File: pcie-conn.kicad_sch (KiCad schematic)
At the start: 22 parts, among them J2 Bus_M.2_1-2199230-6

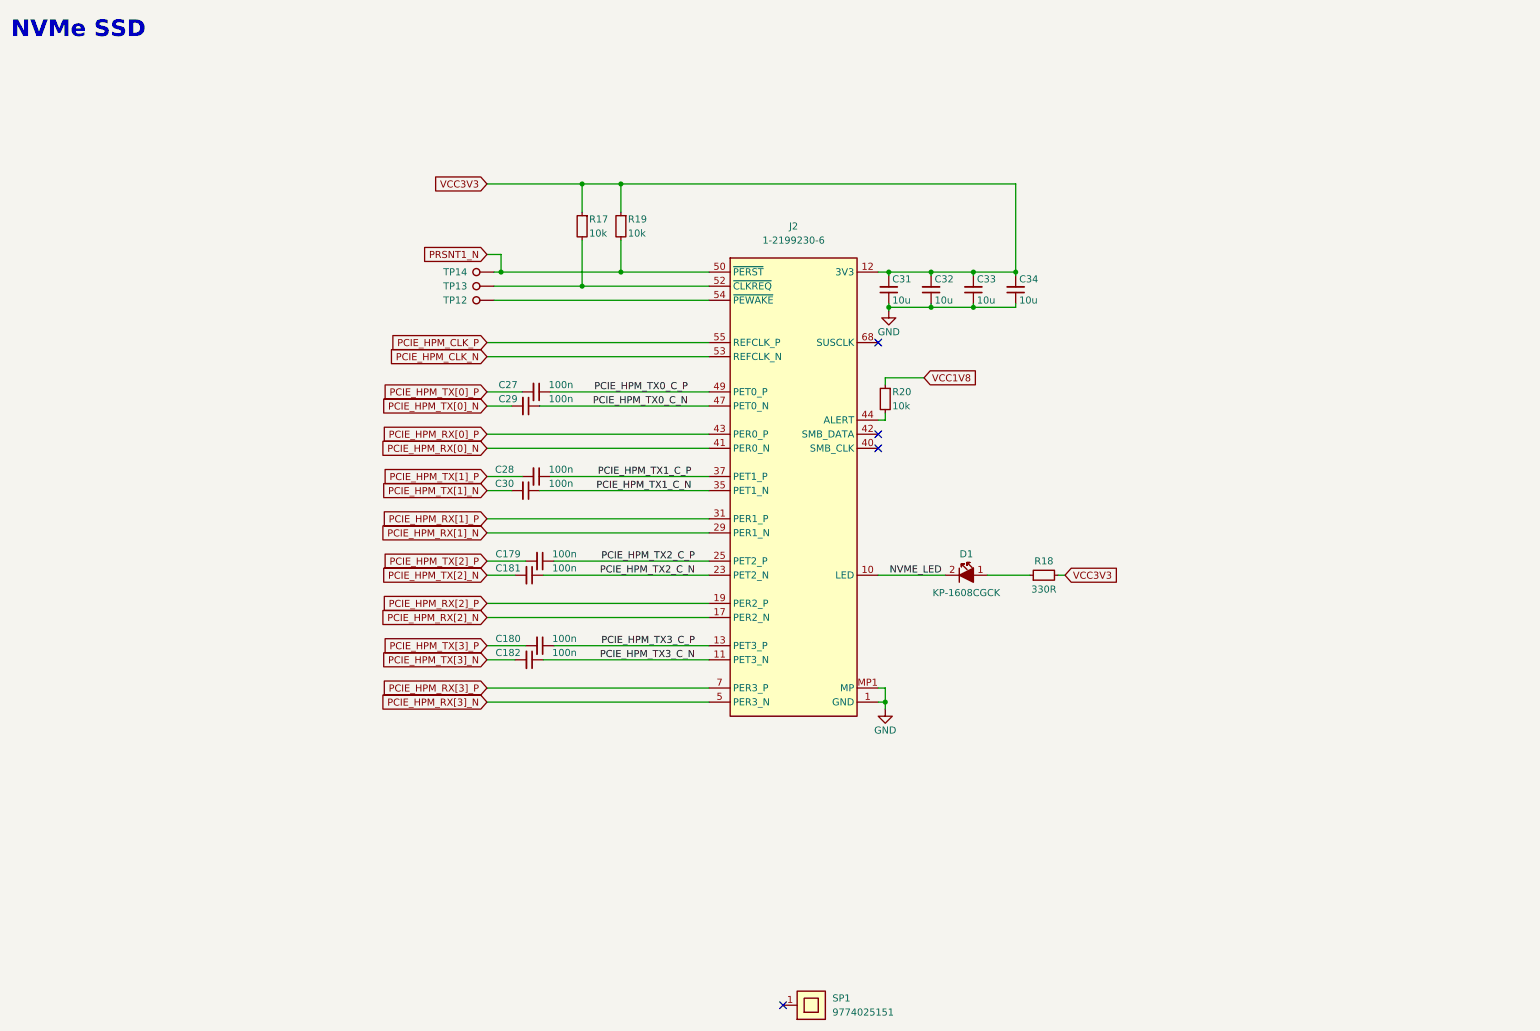
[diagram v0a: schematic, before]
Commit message: [#55652] Fix hotareas
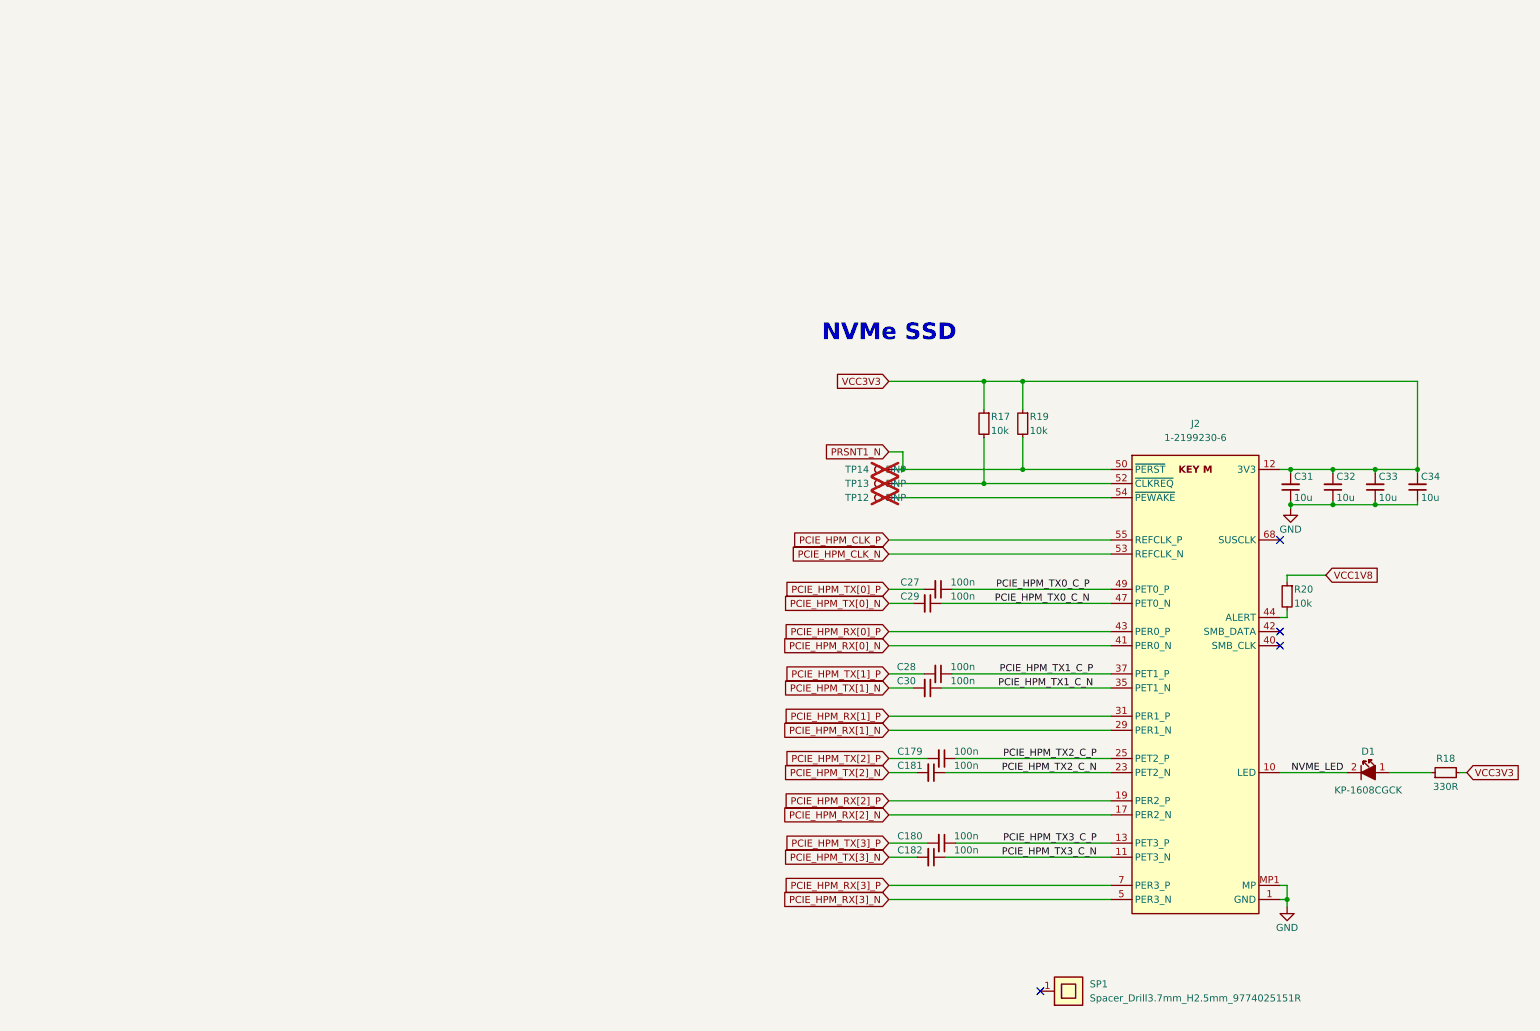
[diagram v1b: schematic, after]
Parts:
- C31, C32, C33, C34: Manufacturer Yaego -> YAGEO
- J2: VSD_Class (none) -> M.2 Key M
- SP1: value Spacer_H2.5mm_9774025151 -> Spacer_Drill3.7mm_H2.5mm_9774025151R; footprint antmicro-footprints:Spacer_SMD_M2.5_H2.5mm_Wurth_9774025151 -> antmicro-footprints:Spacer_Drill3.7mm_H2.5mm_9774025151R; symbol antmicroMechanicalParts:Spacer_H2.5mm_9774025151 -> antmicroMechanicalParts:Spacer_Drill3.7mm_H2.5mm_9774025151R; MPN 9774025151 -> 9774025151R
- TP12, TP13, TP14: value TP_SMD1MM -> TP_1mm_SMD; footprint antmicro-footprints:Testpoint_smd_1mm -> antmicro-footprints:TP_SMD_1mm; now not fitted; now left out of the parts list
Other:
- moved on the sheet: C179, C180, C181, C182, C27, C28, C29, C30, C31, C32, C33, C34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

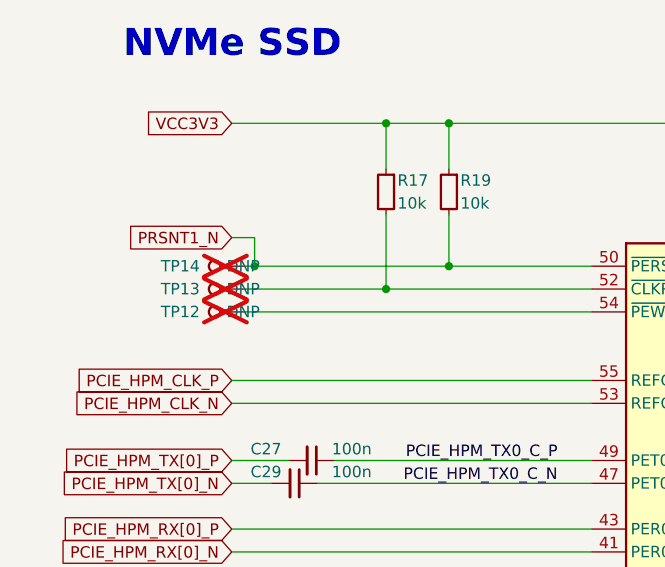
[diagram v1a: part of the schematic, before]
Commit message: [#68236] Update components description
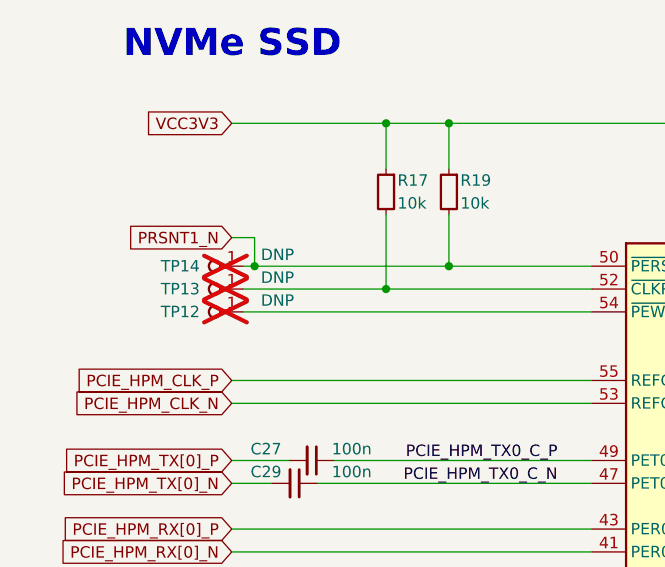
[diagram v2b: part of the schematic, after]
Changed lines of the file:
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@@
     )
   )
-  (symbol (lib_name "C_100n_6V3_0402_3") (lib_id "antmicroCapacitorsmisc:C_100n_6V3_0402") (at 185.42 119.38 180) (unit 1)
+  (symbol (lib_id "antmicroCapacitorsmisc:C_100n_6V3_0402") (at 185.42 119.38 180) (unit 1)
     (in_bom yes) (on_board yes) (dnp no)
     (property "Reference" "C27" (at 177.8 118.11 0)
@@
     )
   )
-  (symbol (lib_name "C_100n_6V3_0402_4") (lib_id "antmicroCapacitorsmisc:C_100n_6V3_0402") (at 183.515 121.92 180) (unit 1)
+  (symbol (lib_id "antmicroCapacitorsmisc:C_100n_6V3_0402") (at 183.515 121.92 180) (unit 1)
     (in_bom yes) (on_board yes) (dnp no)
     (property "Reference" "C29" (at 177.8 120.65 0)
@@
     )
   )
-  (symbol (lib_name "C_100n_6V3_0402_6") (lib_id "antmicroCapacitorsmisc:C_100n_6V3_0402") (at 185.42 134.62 180) (unit 1)
+  (symbol (lib_id "antmicroCapacitorsmisc:C_100n_6V3_0402") (at 185.42 134.62 180) (unit 1)
     (in_bom yes) (on_board yes) (dnp no)
     (property "Reference" "C28" (at 177.165 133.35 0)
@@
     )
   )
-  (symbol (lib_name "C_100n_6V3_0402_7") (lib_id "antmicroCapacitorsmisc:C_100n_6V3_0402") (at 183.515 137.16 180) (unit 1)
+  (symbol (lib_id "antmicroCapacitorsmisc:C_100n_6V3_0402") (at 183.515 137.16 180) (unit 1)
     (in_bom yes) (on_board yes) (dnp no)
     (property "Reference" "C30" (at 177.165 135.89 0)
@@
     )
   )
-  (symbol (lib_name "R_10k_0402_1") (lib_id "antmicroResistors0402:R_10k_0402") (at 191.135 86.995 270) (unit 1)
+  (symbol (lib_id "antmicroResistors0402:R_10k_0402") (at 191.135 86.995 270) (unit 1)
     (in_bom yes) (on_board yes) (dnp no)
     (property "Reference" "R17" (at 192.405 88.265 90)
@@
     )
   )
-  (symbol (lib_name "R_10k_0402_2") (lib_id "antmicroResistors0402:R_10k_0402") (at 198.12 86.995 270) (unit 1)
+  (symbol (lib_id "antmicroResistors0402:R_10k_0402") (at 198.12 86.995 270) (unit 1)
     (in_bom yes) (on_board yes) (dnp no)
     (property "Reference" "R19" (at 199.39 88.265 90)
@@
     )
   )
-  (symbol (lib_name "C_10u_0402_3") (lib_id "antmicroCapacitors0402:C_10u_0402") (at 246.38 103.505 90) (unit 1)
+  (symbol (lib_id "antmicroCapacitors0402:C_10u_0402") (at 246.38 103.505 90) (unit 1)
     (in_bom yes) (on_board yes) (dnp no)
     (property "Reference" "C31" (at 247.015 99.06 90)
@@
     )
   )
-  (symbol (lib_name "C_10u_0402_2") (lib_id "antmicroCapacitors0402:C_10u_0402") (at 261.62 103.505 90) (unit 1)
+  (symbol (lib_id "antmicroCapacitors0402:C_10u_0402") (at 261.62 103.505 90) (unit 1)
     (in_bom yes) (on_board yes) (dnp no)
     (property "Reference" "C33" (at 262.255 99.06 90)
@@
     )
   )
-  (symbol (lib_name "C_10u_0402_1") (lib_id "antmicroCapacitors0402:C_10u_0402") (at 269.24 103.505 90) (unit 1)
+  (symbol (lib_id "antmicroCapacitors0402:C_10u_0402") (at 269.24 103.505 90) (unit 1)
     (in_bom yes) (on_board yes) (dnp no)
     (property "Reference" "C34" (at 269.875 99.06 90)
@@
     )
   )
-  (symbol (lib_name "C_100n_6V3_0402_5") (lib_id "antmicroCapacitorsmisc:C_100n_6V3_0402") (at 186.055 149.86 180) (unit 1)
+  (symbol (lib_id "antmicroCapacitorsmisc:C_100n_6V3_0402") (at 186.055 149.86 180) (unit 1)
     (in_bom yes) (on_board yes) (dnp no)
     (property "Reference" "C179" (at 177.8 148.59 0)
@@
     )
   )
-  (symbol (lib_name "C_100n_6V3_0402_1") (lib_id "antmicroCapacitorsmisc:C_100n_6V3_0402") (at 186.055 165.1 180) (unit 1)
+  (symbol (lib_id "antmicroCapacitorsmisc:C_100n_6V3_0402") (at 186.055 165.1 180) (unit 1)
     (in_bom yes) (on_board yes) (dnp no)
     (property "Reference" "C180" (at 177.8 163.83 0)
@@
     )
   )
-  (symbol (lib_name "C_100n_6V3_0402_2") (lib_id "antmicroCapacitorsmisc:C_100n_6V3_0402") (at 184.15 167.64 180) (unit 1)
+  (symbol (lib_id "antmicroCapacitorsmisc:C_100n_6V3_0402") (at 184.15 167.64 180) (unit 1)
     (in_bom yes) (on_board yes) (dnp no)
     (property "Reference" "C182" (at 177.8 166.37 0)
@@
       (effects (font (size 1.27 1.27) (thickness 0.15)) (justify left bottom) hide)
     )
-    (property "DNP" "DNP" (at 175.26 102.87 0)
+    (property "DNP" "DNP" (at 179.07 101.6 0)
       (effects (font (size 1.27 1.27)))
     )
@@
     )
   )
-  (symbol (lib_name "TP_1mm_SMD_2") (lib_id "antmicroTestPoints:TP_1mm_SMD") (at 175.26 100.33 180) (unit 1)
+  (symbol (lib_id "antmicroTestPoints:TP_1mm_SMD") (at 175.26 100.33 180) (unit 1)
     (in_bom no) (on_board yes) (dnp yes)
     (property "Reference" "TP13" (at 168.275 100.33 0)
@@
       (effects (font (size 1.27 1.27) (thickness 0.15)) (justify left bottom) hide)
     )
-    (property "DNP" "DNP" (at 175.26 100.33 0)
+    (property "DNP" "DNP" (at 179.07 99.06 0)
       (effects (font (size 1.27 1.27)))
     )
@@
     )
   )
-  (symbol (lib_name "TP_1mm_SMD_1") (lib_id "antmicroTestPoints:TP_1mm_SMD") (at 175.26 97.79 0) (mirror y) (unit 1)
+  (symbol (lib_id "antmicroTestPoints:TP_1mm_SMD") (at 175.26 97.79 0) (mirror y) (unit 1)
     (in_bom no) (on_board yes) (dnp yes)
     (property "Reference" "TP14" (at 168.275 97.79 0)
@@
       (effects (font (size 1.27 1.27) (thickness 0.15)) (justify left bottom) hide)
     )
-    (property "DNP" "DNP" (at 175.26 97.79 0)
-      (effects (font (size 1.27 1.27)))
-    )
+    (property "DNP" "DNP" (at 179.07 96.52 0)
+      (effects (font (size 1.27 1.27)))
+    )

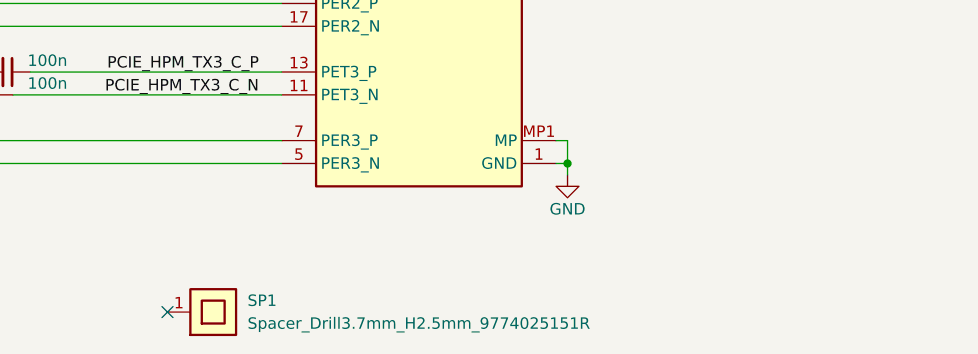
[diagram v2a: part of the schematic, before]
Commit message: [#68236] Change studs reference from SP to H
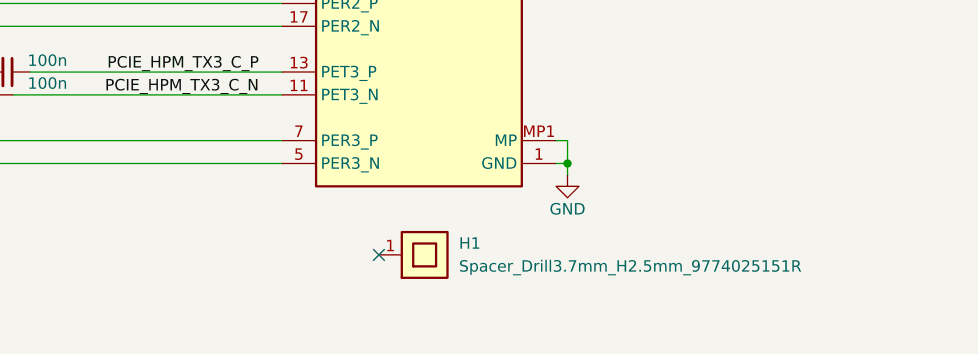
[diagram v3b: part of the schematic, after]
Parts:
- removed SP1: Spacer_Drill3.7mm_H2.5mm_9774025151R, antmicro-footprints:Spacer_Drill3.7mm_H2.5mm_9774025151R, symbol antmicroMechanicalParts:Spacer_Drill3.7mm_H2.5mm_9774025151R
- added H1: Spacer_Drill3.7mm_H2.5mm_9774025151R, antmicro-footprints:Spacer_Drill3.7mm_H2.5mm_9774025151R, symbol antmicroMechanicalParts:Spacer_Drill3.7mm_H2.5mm_9774025151R
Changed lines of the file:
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@@
   (junction (at 198.12 81.915) (diameter 0) (color 0 0 0 0)
   )
-  (no_connect (at 201.295 191.77))
   (no_connect (at 244.475 127))
   (no_connect (at 244.475 129.54))
+  (no_connect (at 224.79 185.42))
   (no_connect (at 244.475 110.49))
   (wire (pts (xy 180.34 134.62) (xy 173.99 134.62))
@@
     )
   )
-  (symbol (lib_id "antmicroMechanicalParts:Spacer_Drill3.7mm_H2.5mm_9774025151R") (at 201.295 191.77 0) (unit 1)
-    (in_bom yes) (on_board yes) (dnp no)
-    (property "Reference" "SP1" (at 210.185 190.5 0)
-      (effects (font (size 1.27 1.27)) (justify left))
-    )
-    (property "Value" "Spacer_Drill3.7mm_H2.5mm_9774025151R" (at 210.185 193.04 0)
-      (effects (font (size 1.27 1.27) (thickness 0.15)) (justify left))
-    )
-    (property "Footprint" "antmicro-footprints:Spacer_Drill3.7mm_H2.5mm_9774025151R" (at 224.155 199.39 0)
-      (effects (font (size 1.27 1.27) (thickness 0.15)) (justify left bottom) hide)
-    )
-    (property "Datasheet" "https://www.we-online.com/components/products/datasheet/9774025151R.pdf" (at 224.155 201.93 0)
-      (effects (font (size 1.27 1.27) (thickness 0.15)) (justify left bottom) hide)
-    )
-    (property "Manufacturer" "Würth Elektronik" (at 224.155 204.47 0)
-      (effects (font (size 1.27 1.27) (thickness 0.15)) (justify left bottom) hide)
-    )
-    (property "MPN" "9774025151R" (at 224.155 207.01 0)
-      (effects (font (size 1.27 1.27) (thickness 0.15)) (justify left bottom) hide)
-    )
-    (property "Author" "Antmicro" (at 224.155 209.55 0)
-      (effects (font (size 1.27 1.27) (thickness 0.15)) (justify left bottom) hide)
-    )
-    (property "License" "Apache-2.0" (at 224.155 212.09 0)
-      (effects (font (size 1.27 1.27) (thickness 0.15)) (justify left bottom) hide)
-    )
-    (pin "1")
-    (instances
-      (project "artix-dc-scm"
-        (path "/f3cd042e-9a46-4397-9768-c62eb1c291be/00000000-0000-0000-0000-00005fd17ef1"
-          (reference "SP1") (unit 1)
-        )
-      )
-    )
-  )
   (symbol (lib_id "antmicropower:GND") (at 245.745 176.53 0) (unit 1)
     (in_bom yes) (on_board yes) (dnp no)
@@
         )
       )
+    )
+  )
+  (symbol (lib_id "antmicroMechanicalParts:Spacer_Drill3.7mm_H2.5mm_9774025151R") (at 224.79 185.42 0) (unit 1)
+    (in_bom yes) (on_board yes) (dnp no) (fields_autoplaced)
+    (property "Reference" "H1" (at 233.68 184.15 0)
+      (effects (font (size 1.27 1.27) (thickness 0.15)) (justify left))
+    )
+    (property "Value" "Spacer_Drill3.7mm_H2.5mm_9774025151R" (at 233.68 186.69 0)
+      (effects (font (size 1.27 1.27) (thickness 0.15)) (justify left))
+    )
+    (property "Footprint" "antmicro-footprints:Spacer_Drill3.7mm_H2.5mm_9774025151R" (at 247.65 193.04 0)
+      (effects (font (size 1.27 1.27) (thickness 0.15)) (justify left bottom) hide)
+    )
+    (property "Datasheet" "https://www.we-online.com/components/products/datasheet/9774025151R.pdf" (at 247.65 195.58 0)
+      (effects (font (size 1.27 1.27) (thickness 0.15)) (justify left bottom) hide)
+    )
+    (property "Manufacturer" "Würth Elektronik" (at 247.65 198.12 0)
+      (effects (font (size 1.27 1.27) (thickness 0.15)) (justify left bottom) hide)
+    )
+    (property "MPN" "9774025151R" (at 247.65 200.66 0)
+      (effects (font (size 1.27 1.27) (thickness 0.15)) (justify left bottom) hide)
+    )
+    (property "Author" "Antmicro" (at 247.65 203.2 0)
+      (effects (font (size 1.27 1.27) (thickness 0.15)) (justify left bottom) hide)
+    )
+    (property "License" "Apache-2.0" (at 247.65 205.74 0)
+      (effects (font (size 1.27 1.27) (thickness 0.15)) (justify left bottom) hide)
+    )
+    (pin "1")
+    (instances
+      (project "artix-dc-scm"
+        (path "/f3cd042e-9a46-4397-9768-c62eb1c291be/00000000-0000-0000-0000-00005fd17ef1"
+          (reference "H1") (unit 1)
+        )
+      )
